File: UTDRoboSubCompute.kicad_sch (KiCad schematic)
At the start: 51 parts, among them IC1 TPD4E05U06QDQARQ1, IC2 TPD4E05U06QDQARQ1, J1 Disable Bluetooth/Wifi, J10 HEADER-3X04, J11 HEADER-3X04, J12 HEADER-3X04, J13 Conn_02x20_Odd_Even, J14 GSB3116344KHHR, J15 GSB3116344KHHR, J16 TF38-22S-0.5SV_830_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

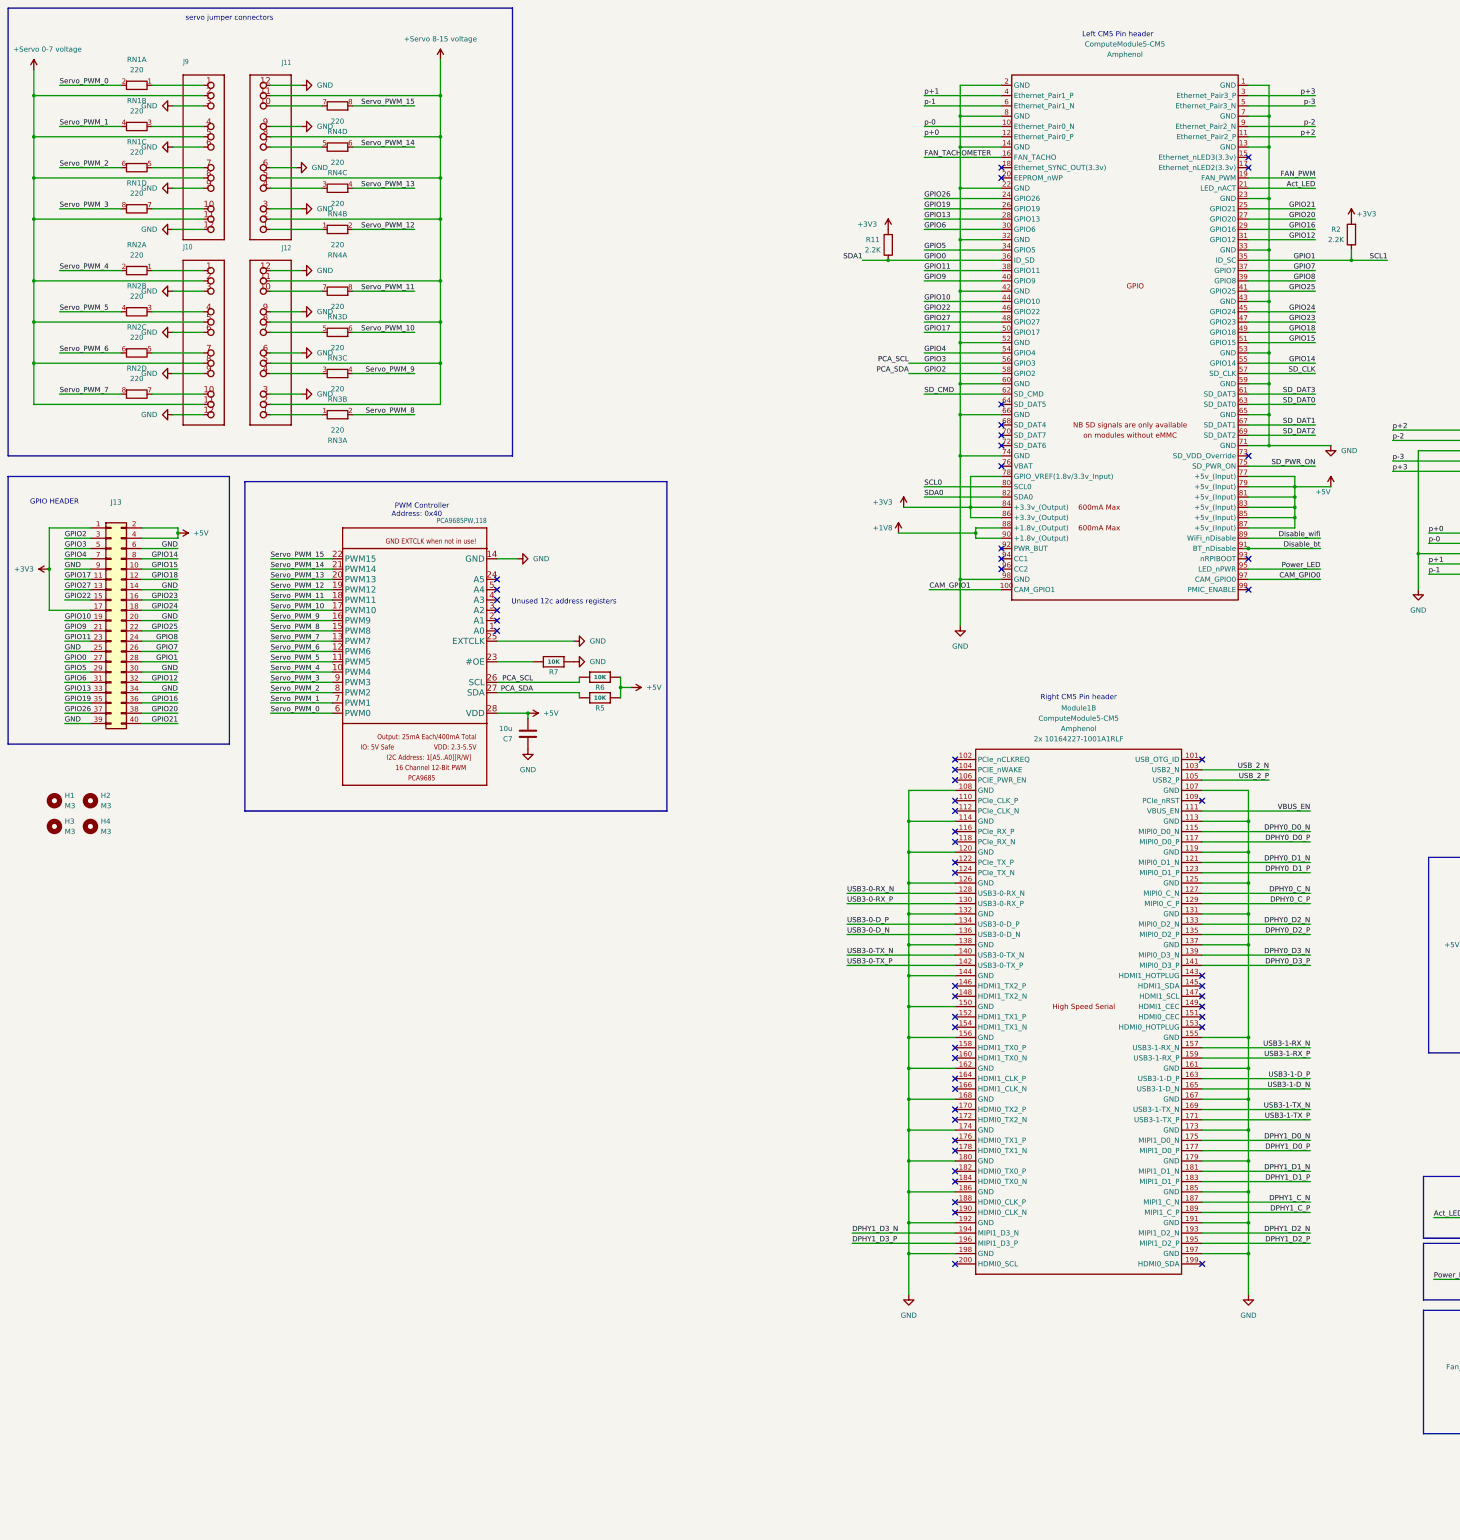
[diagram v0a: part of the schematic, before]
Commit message: Improve README and update PCB sheet/net refs
Expanded and clarified README: added table of contents, more component details (servo, CSI/DSI, Ethernet, USB, SD boot, power, fan), images, USB config hint (dtoverlay), PCB dimensions, and a recommendation to use the interactive BOM. Updated UTDRoboSubCompute.kicad_pcb: replaced many sheetfile references from cm5testcarrier.kicad_sch to UTDRoboSubCompute.kicad_sch, ), adjusted a pad reference, and refreshed numerous footprint UUIDs. These changes align documentation with the board files and fix net/sheet references used by the PCB and BOM generation.
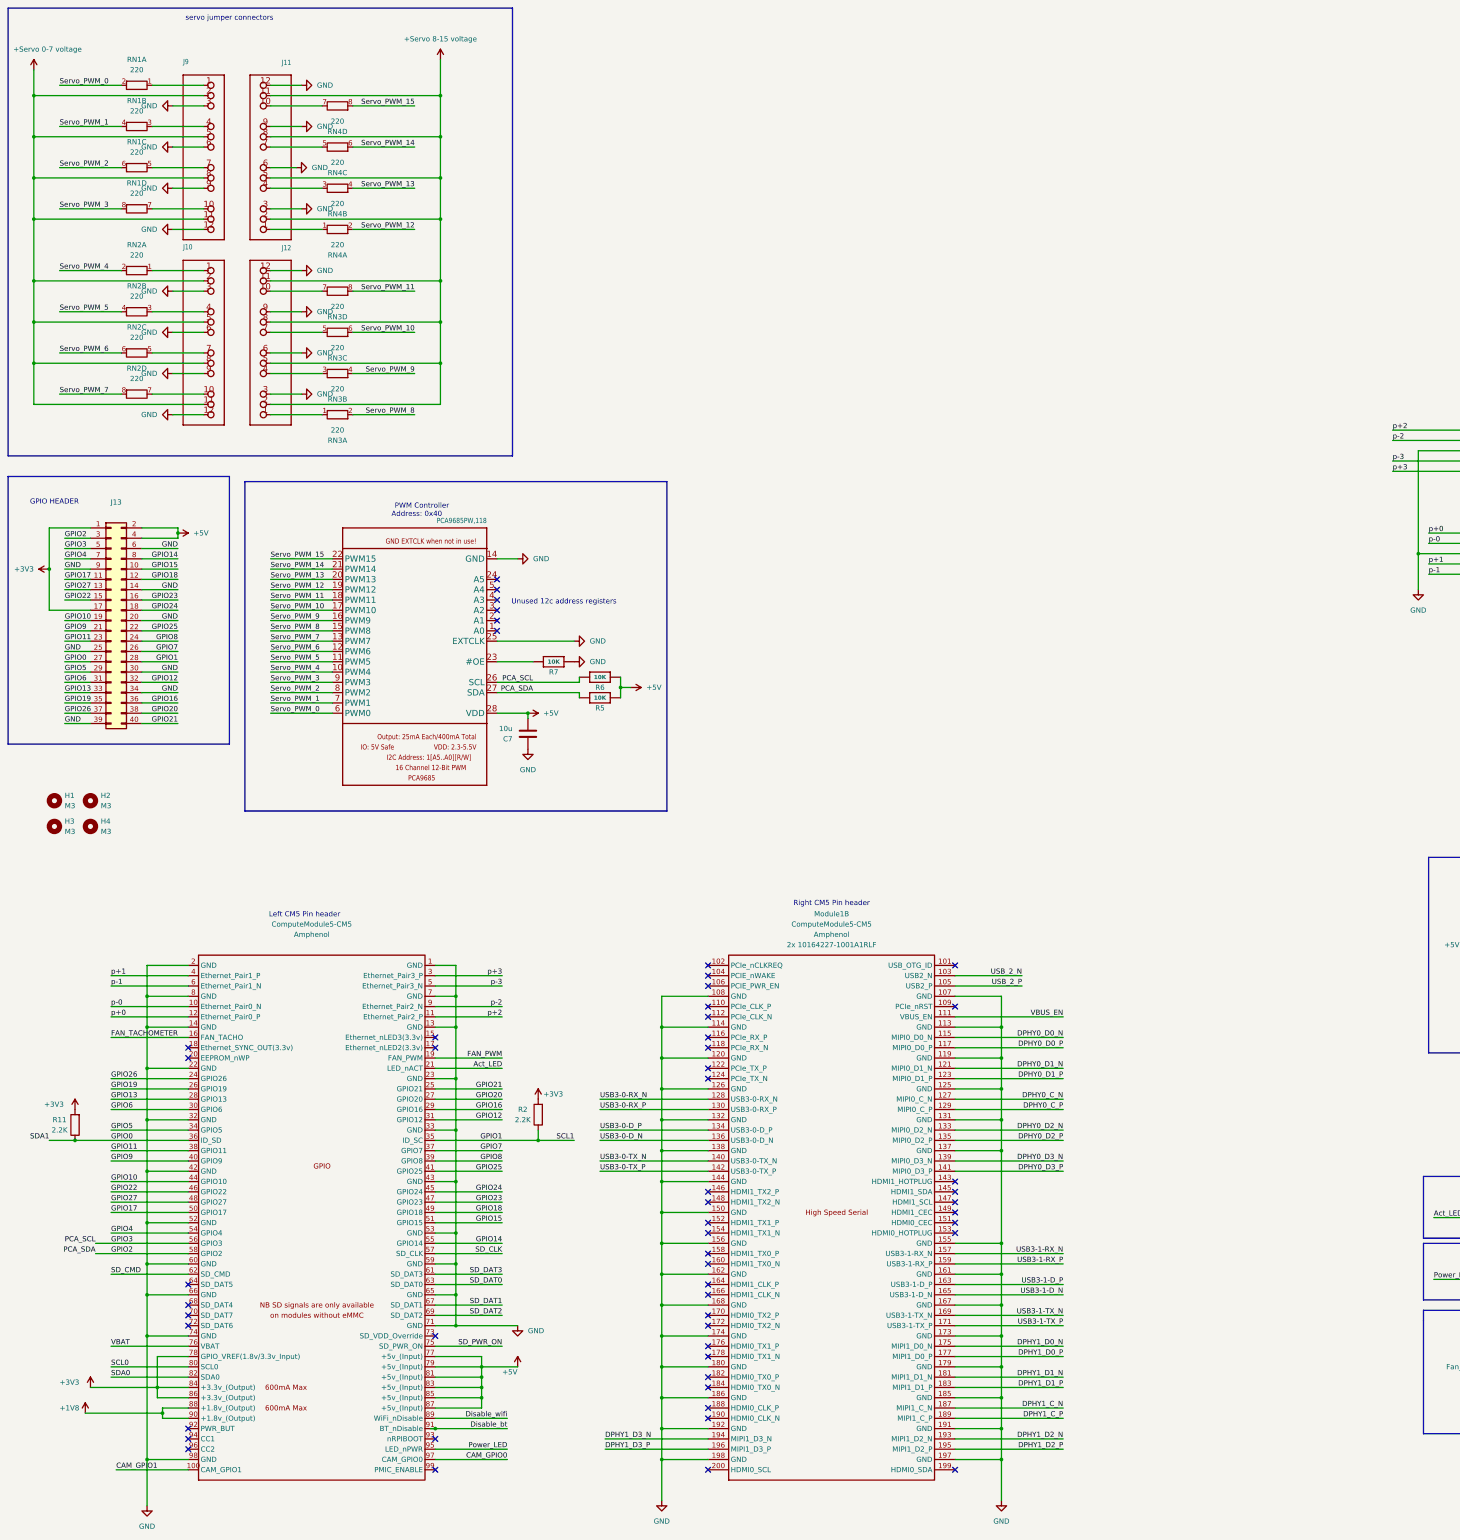
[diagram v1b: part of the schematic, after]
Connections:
- net VBAT: now reaches Module1.76 (VBAT)
- no-connect marks 60 -> 59
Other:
- moved on the sheet: Module1B, R11, R2

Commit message: Better trace spacing, JLCPCB compliant & misc fixes
 - Added JLCPCB rules file
 - Made design JLCPCB compliant
 - updated README.md with additional details about diff and non-diff trace routing
 - updated images in README.md
 - updated clearance specs for signaling lines to 3*W
 - flipped GPIO header and reflected spacing changes in routing
 - Fixed Servo Address register floating pins issue
 - Fixed 3.3v input on SD power IC non-connection
 - rerouted servo PWM lines for better spacing
 - rerouted SD card data lines for better spacing, and clearer routes
 - Switched Servo Power Traces to fills in order to allow for multi-layer connections
 - added extra pads for bulk capacitors
 - added more descriptive silkscreens
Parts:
- added C10, C8, C9: ~, Capacitor_SMD:C_0805_2012Metric_Pad1.18x1.45mm_HandSolder, symbol Device:C
- C4: symbol Device:C_Polarized -> Device:C
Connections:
- net +3.3v is gone; now on net +3V3: R10.1, U2.5 (IN)
- net +5V: now also C10.2, C8.2, C9.2
- net GND: now also U4.1 (A0), U4.2 (A1), U4.24 (A5), U4.3 (A2), U4.4 (A3), U4.5 (A4), C10.1, C8.1, C9.1
- no-connect marks 59 -> 53
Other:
- note added: "Extra Cap Pads"
- note added: "Pull down for Address 0"
- note removed: "Unused 12c address registers"
- note removed: "pin name mistmatch ;("
- moved on the sheet: C2, C5, C6, R5, R6

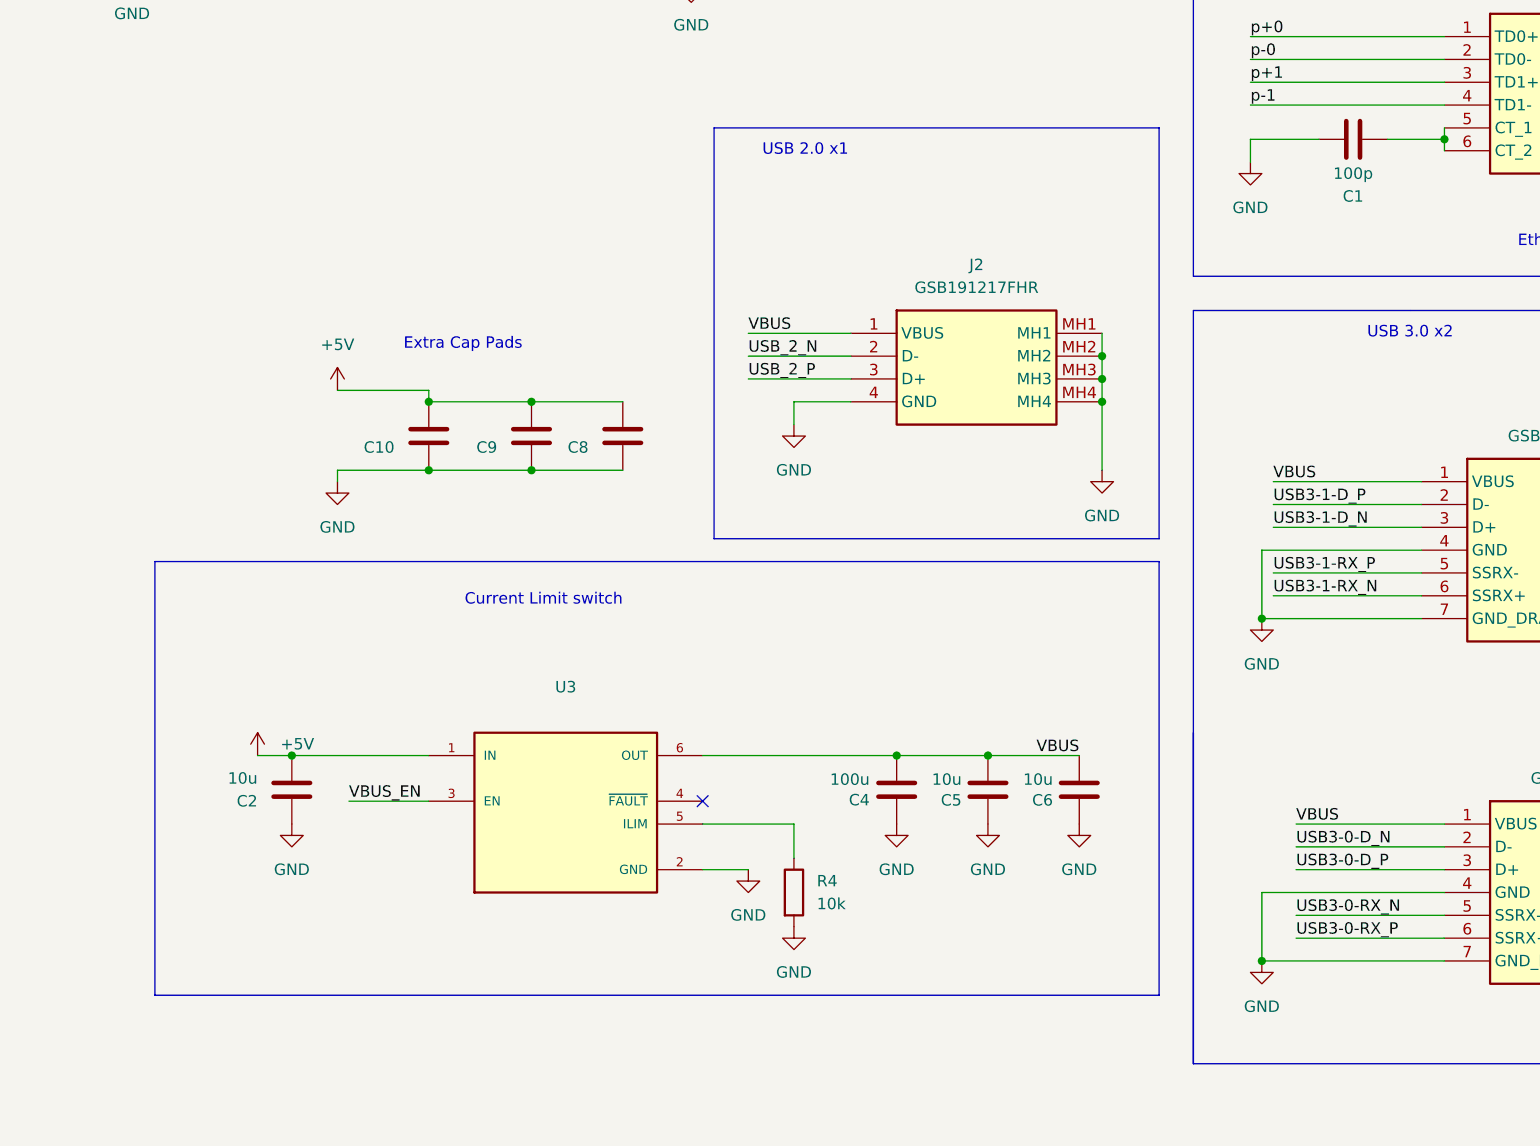
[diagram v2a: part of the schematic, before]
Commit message: Added and adjusted decoupling caps
- added decoupling capacitors to the USB IC
- corrected the value of the center tap decoupling capacitor
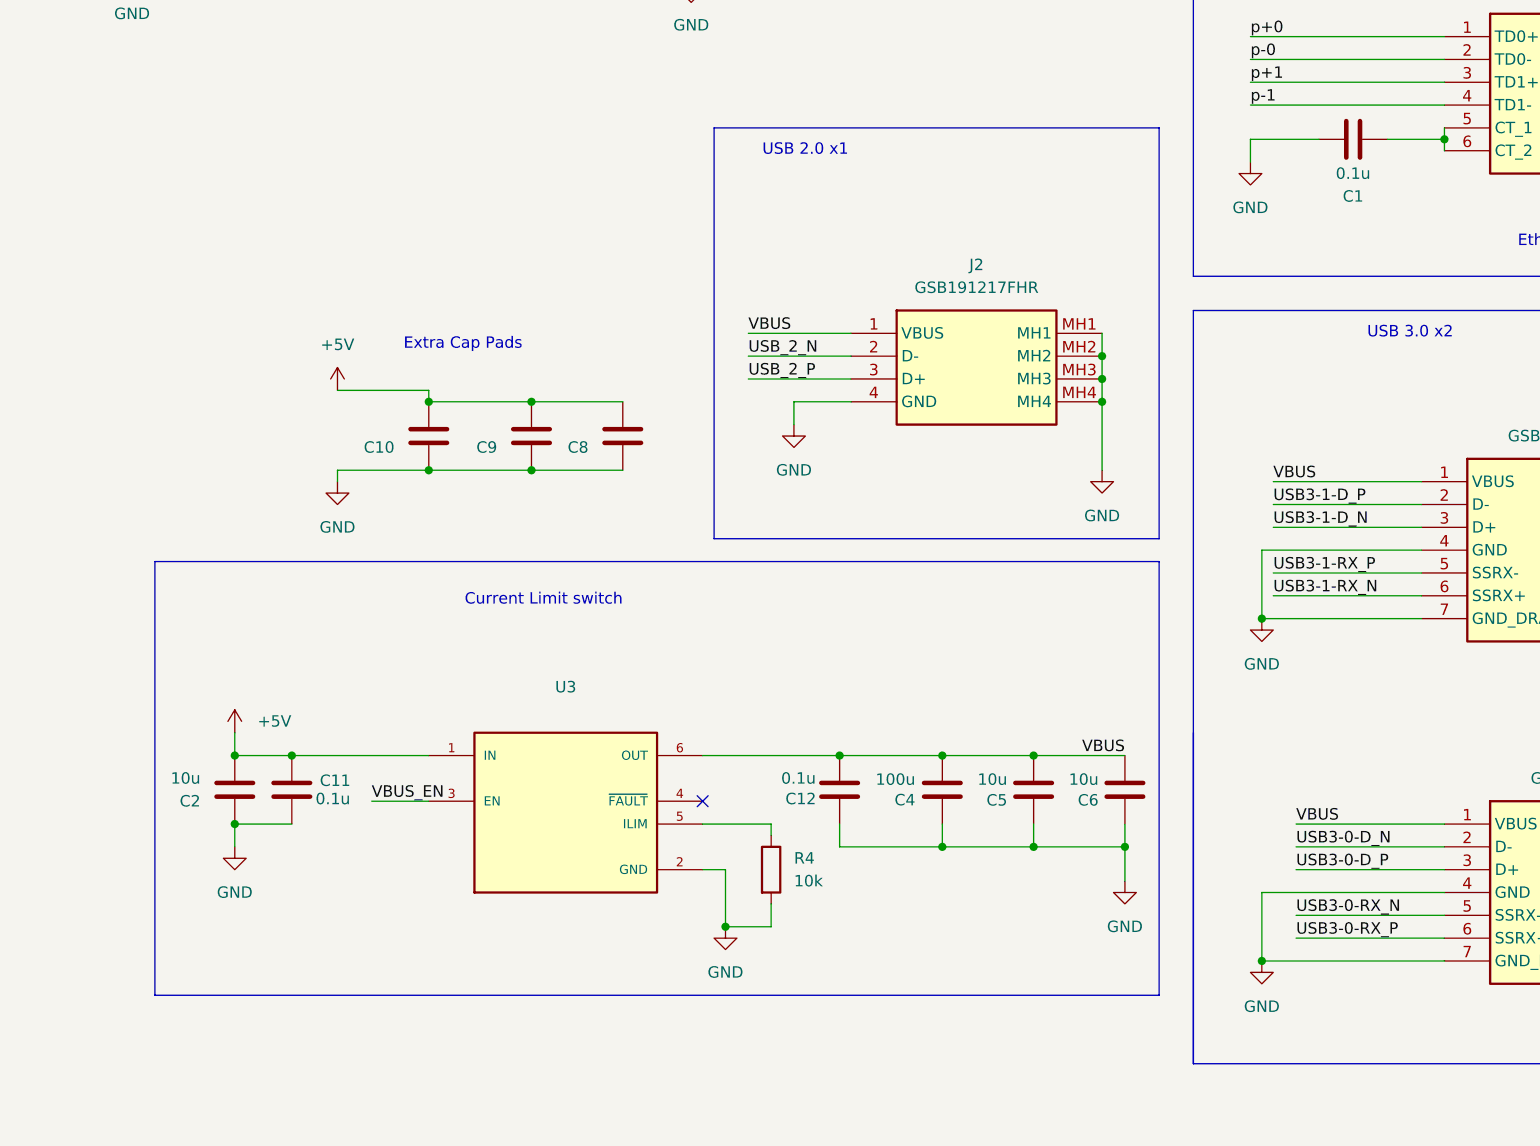
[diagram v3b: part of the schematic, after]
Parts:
- added C11, C12: 0.1u, PCM_Capacitor_SMD_AKL:C_0805_2012Metric_Pad1.15x1.40mm_HandSolder, symbol Device:C
- C1: value 100p -> 0.1u
- C10, C8, C9: value ~ -> (none)
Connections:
- net +5V: now also C11.2
- net GND: now also C11.1, C12.1
- net VBUS: now also C12.2
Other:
- moved on the sheet: C2, C4, C5, C6, R4
